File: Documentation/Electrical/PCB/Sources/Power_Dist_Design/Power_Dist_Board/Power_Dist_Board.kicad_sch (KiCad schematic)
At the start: 62 parts, among them J1 Battery Connector, J10 GND_Bridge_3, J2 5V_Power_Rail, J3 5V_Power_Rail, J4 3.3V_Power_Rail, J5 3.3V_Power_Rail, J6 GND_Rail, J7 GND_Rail, J8 GND_Bridge_1, J9 GND_Bridge_2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

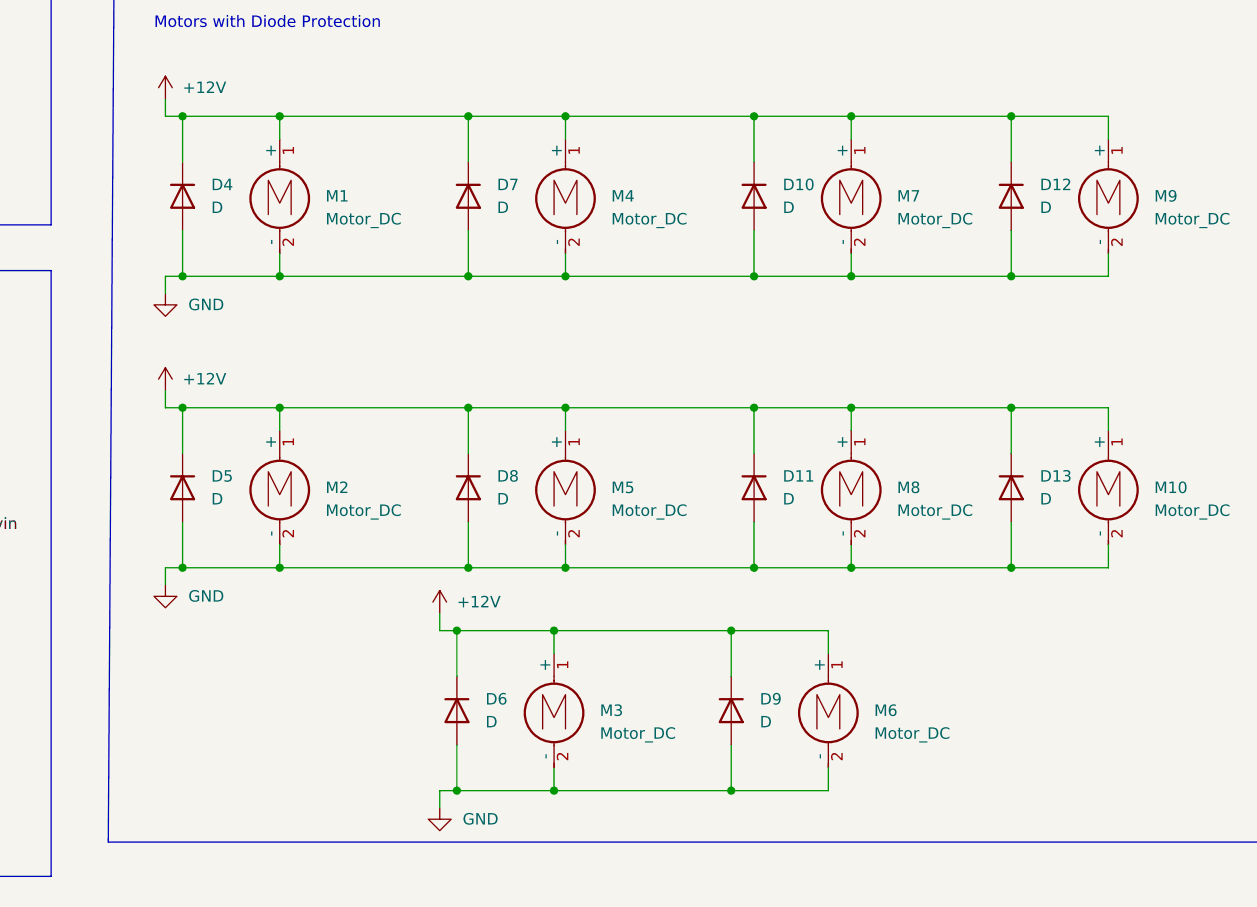
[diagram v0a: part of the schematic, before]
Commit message: added 3d models to pcb
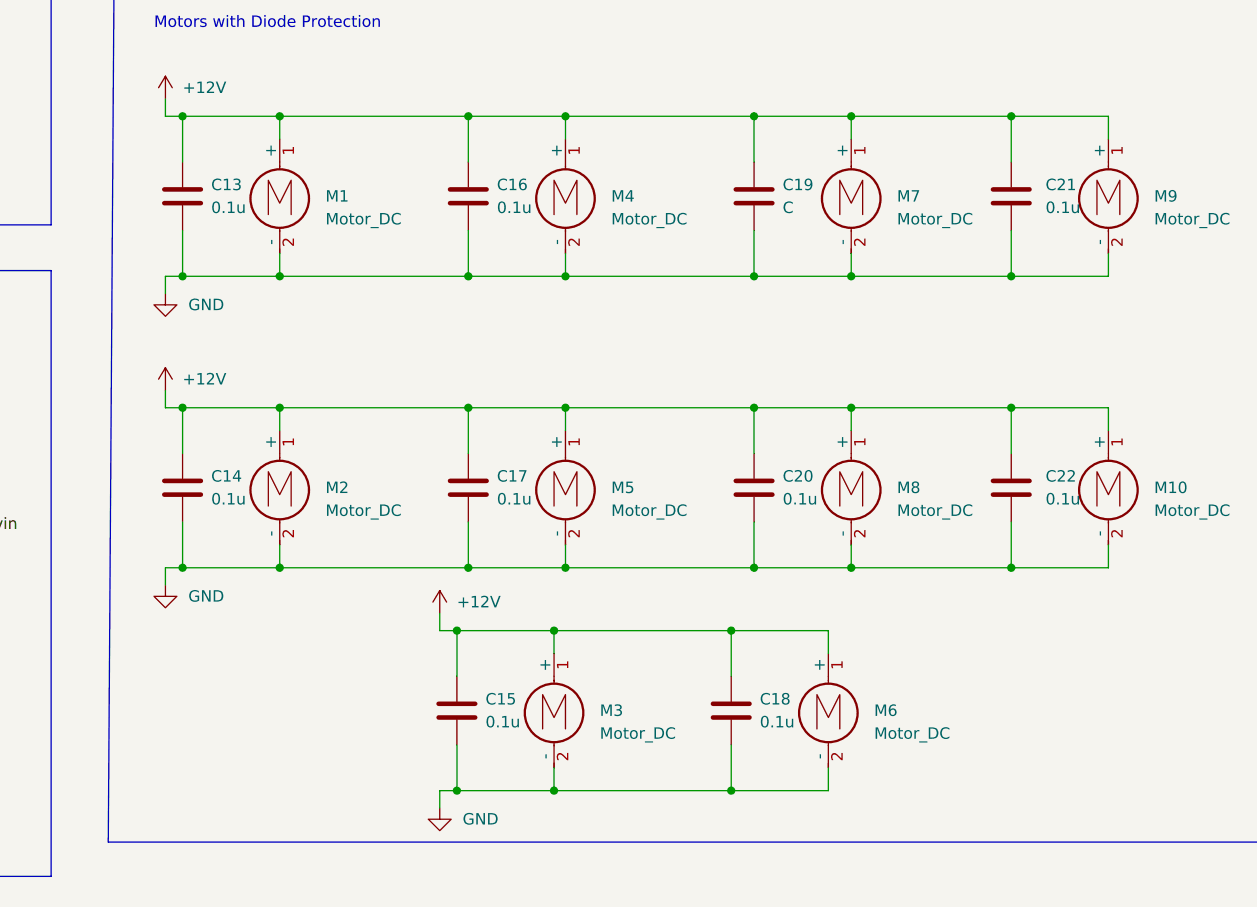
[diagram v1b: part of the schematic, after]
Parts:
- C13: renamed from D4; value D -> 0.1u; footprint RB070MM:DIO_RB051MM_ROM-M -> Capacitor_SMD:C_1206_3216Metric_Pad1.33x1.80mm_HandSolder; symbol Device:D -> Device:C
- C14: renamed from D5; value D -> 0.1u; footprint RB070MM:DIO_RB051MM_ROM-M -> Capacitor_SMD:C_1206_3216Metric_Pad1.33x1.80mm_HandSolder; symbol Device:D -> Device:C
- C15: renamed from D6; value D -> 0.1u; footprint RB070MM:DIO_RB051MM_ROM-M -> Capacitor_SMD:C_1206_3216Metric_Pad1.33x1.80mm_HandSolder; symbol Device:D -> Device:C
- C16: renamed from D7; value D -> 0.1u; footprint RB070MM:DIO_RB051MM_ROM-M -> Capacitor_SMD:C_1206_3216Metric_Pad1.33x1.80mm_HandSolder; symbol Device:D -> Device:C
- C17: renamed from D8; value D -> 0.1u; footprint RB070MM:DIO_RB051MM_ROM-M -> Capacitor_SMD:C_1206_3216Metric_Pad1.33x1.80mm_HandSolder; symbol Device:D -> Device:C
- C18: renamed from D9; value D -> 0.1u; footprint RB070MM:DIO_RB051MM_ROM-M -> Capacitor_SMD:C_1206_3216Metric_Pad1.33x1.80mm_HandSolder; symbol Device:D -> Device:C
- C19: renamed from D10; value D -> C; footprint RB070MM:DIO_RB051MM_ROM-M -> Capacitor_SMD:C_1206_3216Metric_Pad1.33x1.80mm_HandSolder; symbol Device:D -> Device:C
- C20: renamed from D11; value D -> 0.1u; footprint RB070MM:DIO_RB051MM_ROM-M -> Capacitor_SMD:C_1206_3216Metric_Pad1.33x1.80mm_HandSolder; symbol Device:D -> Device:C
- C21: renamed from D12; value D -> 0.1u; footprint RB070MM:DIO_RB051MM_ROM-M -> Capacitor_SMD:C_1206_3216Metric_Pad1.33x1.80mm_HandSolder; symbol Device:D -> Device:C
- C22: renamed from D13; value D -> 0.1u; footprint RB070MM:DIO_RB051MM_ROM-M -> Capacitor_SMD:C_1206_3216Metric_Pad1.33x1.80mm_HandSolder; symbol Device:D -> Device:C

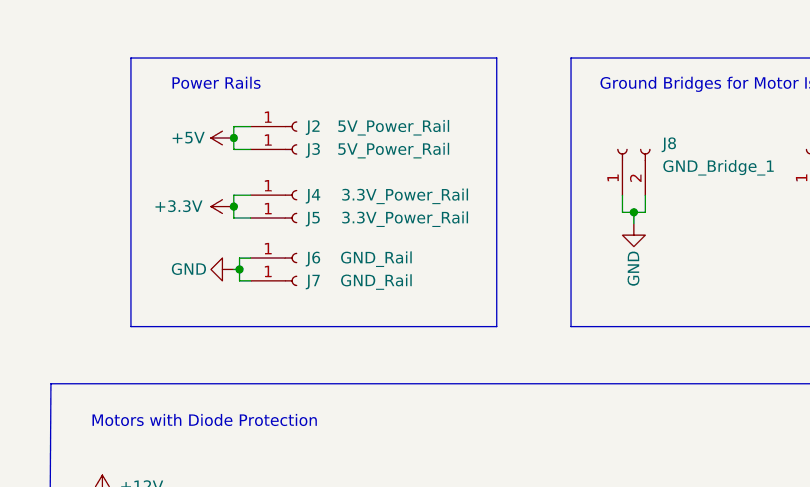
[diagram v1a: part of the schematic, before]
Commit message: small changes to power pcb
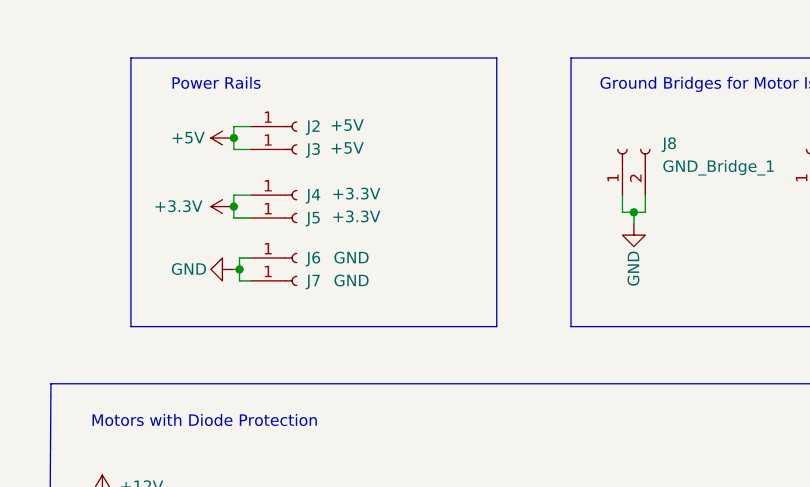
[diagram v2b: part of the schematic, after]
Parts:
- J2, J3: value 5V_Power_Rail -> +5V
- J4, J5: value 3.3V_Power_Rail -> +3.3V
- J6, J7: value GND_Rail -> GND
- L1, L2: footprint L_TDK_SPM6530:IND_SPM6530_TDK -> Power_Dist:IND_SPM6530_TDK
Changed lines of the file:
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@@
       (effects (font (size 1.27 1.27)))
     )
-    (property "Footprint" "L_TDK_SPM6530:IND_SPM6530_TDK" (at 62.23 119.38 0)
+    (property "Footprint" "Power_Dist:IND_SPM6530_TDK" (at 62.23 119.38 0)
       (effects (font (size 1.27 1.27)) hide)
     )
@@
       (effects (font (size 1.27 1.27)))
     )
-    (property "Value" "3.3V_Power_Rail" (at 189.865 40.005 0)
+    (property "Value" "+3.3V" (at 184.404 39.878 0)
       (effects (font (size 1.27 1.27)))
     )
@@
       (effects (font (size 1.27 1.27)))
     )
-    (property "Value" "3.3V_Power_Rail" (at 189.865 37.465 0)
+    (property "Value" "+3.3V" (at 184.404 37.338 0)
       (effects (font (size 1.27 1.27)))
     )
@@
       (effects (font (size 1.27 1.27)))
     )
-    (property "Value" "5V_Power_Rail" (at 188.595 32.385 0)
+    (property "Value" "+5V" (at 183.388 32.258 0)
       (effects (font (size 1.27 1.27)))
     )
@@
       (effects (font (size 1.27 1.27)))
     )
-    (property "Value" "5V_Power_Rail" (at 188.595 29.845 0)
+    (property "Value" "+5V" (at 183.388 29.718 0)
       (effects (font (size 1.27 1.27)))
     )
@@
       (effects (font (size 1.27 1.27)))
     )
-    (property "Footprint" "L_TDK_SPM6530:IND_SPM6530_TDK" (at 62.23 46.99 0)
+    (property "Footprint" "Power_Dist:IND_SPM6530_TDK" (at 62.23 46.99 0)
       (effects (font (size 1.27 1.27)) hide)
     )
@@
       (effects (font (size 1.27 1.27)))
     )
-    (property "Value" "GND_Rail" (at 186.69 46.99 0)
+    (property "Value" "GND" (at 183.896 46.99 0)
       (effects (font (size 1.27 1.27)))
     )
@@
       (effects (font (size 1.27 1.27)))
     )
-    (property "Value" "GND_Rail" (at 186.69 44.45 0)
-      (effects (font (size 1.27 1.27)))
-    )
+    (property "Value" "GND" (at 183.896 44.45 0)
+      (effects (font (size 1.27 1.27)))
+    )

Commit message: added schematic of power board as pdf
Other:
- note added: "Emergency Stop Button"
- note added: "Motors with Protection"
- note removed: "Motors with Diode Protection"
- moved on the sheet: J10, J2, J3, J4, J5, J6, J7, J8, J9
